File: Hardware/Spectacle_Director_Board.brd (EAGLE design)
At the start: 25.4 x 55.9 mm, 57 parts, among them J1 AUDIO-JACK3, J2 CORTEX_DEBUGPTH, Q1 2N7002PW, Q2 2N7002PW, U3 AP2112K-3.3V, U4 ATSAMD21G-A, U5 W25Q32FVSS

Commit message: Cleaning up schematic
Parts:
- TP1: value TEST-POINT3X5 -> TP-SWDIO
- TP2: value TEST-POINT3X5 -> TP-SWCLK
- TP3: value TEST-POINT3X5 -> TP-!RESET!
- TP4: value TEST-POINT3X5 -> TP-3.3V
- TP5: value TEST-POINT3X5 -> TP-GND
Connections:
- removed net A0: U4.3
- removed net A1: U4.7
- removed net A2: U4.8
- removed net A3: U4.9
- removed net A5: U4.47
- removed net AREF: U4.4
- removed net D11: U4.25
- removed net D2: U4.23
- removed net D5: U4.24
- removed net PB22: U4.37
- removed net PB23: U4.38
- removed net USB_HOST_EN: U4.41
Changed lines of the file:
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@@
 <layer number="47" name="Measures" color="7" fill="1" visible="no" active="yes"/>
 <layer number="48" name="Document" color="7" fill="1" visible="no" active="yes"/>
-<layer number="49" name="Reference" color="7" fill="1" visible="yes" active="yes"/>
+<layer number="49" name="Reference" color="7" fill="1" visible="no" active="yes"/>
 <layer number="51" name="tDocu" color="6" fill="1" visible="yes" active="yes"/>
 <layer number="52" name="bDocu" color="7" fill="1" visible="no" active="yes"/>
@@
 <attribute name="PROD_ID" value="RES-07828" x="-8.255" y="41.91" size="1.778" layer="27" font="vector" ratio="15" display="off"/>
 </element>
-<element name="TP1" library="SparkFun-Connectors" package="PAD.03X.05" value="TEST-POINT3X5" x="3.683" y="28.575" rot="MR0"/>
-<element name="TP2" library="SparkFun-Connectors" package="PAD.03X.05" value="TEST-POINT3X5" x="5.588" y="28.575" rot="MR0"/>
-<element name="TP3" library="SparkFun-Connectors" package="PAD.03X.05" value="TEST-POINT3X5" x="7.493" y="28.575" rot="MR0"/>
+<element name="TP1" library="SparkFun-Connectors" package="PAD.03X.05" value="TP-SWDIO" x="3.683" y="28.575" rot="MR0"/>
+<element name="TP2" library="SparkFun-Connectors" package="PAD.03X.05" value="TP-SWCLK" x="5.588" y="28.575" rot="MR0"/>
+<element name="TP3" library="SparkFun-Connectors" package="PAD.03X.05" value="TP-!RESET!" x="7.493" y="28.575" rot="MR0"/>
 <element name="LOGO3" library="SparkFun-Aesthetics" package="SFE_LOGO_FLAME_COPPER_EXPOSED_.2" value="SFE_LOGO_FLAME.2EXP" x="11.43" y="1.27" rot="R90"/>
 <element name="U$1" library="SparkFun-Aesthetics" package="ORDERING_INSTRUCTIONS" value="" x="-16.51" y="-24.13"/>
-<element name="TP4" library="SparkFun-Connectors" package="PAD.03X.05" value="TEST-POINT3X5" x="1.778" y="28.575" rot="MR0"/>
-<element name="TP5" library="SparkFun-Connectors" package="PAD.03X.05" value="TEST-POINT3X5" x="9.398" y="28.575" rot="MR0"/>
+<element name="TP4" library="SparkFun-Connectors" package="PAD.03X.05" value="TP-3.3V" x="1.778" y="28.575" rot="MR0"/>
+<element name="TP5" library="SparkFun-Connectors" package="PAD.03X.05" value="TP-GND" x="9.398" y="28.575" rot="MR0"/>
 <element name="J2" library="SparkFun-Connectors" package="2X5-PTH-1.27MM" value="CORTEX_DEBUGPTH" x="5.588" y="25.908"/>
 </elements>
@@
 <wire x1="13.5024" y1="41.4678" x2="13.2334" y2="41.1988" width="0.2032" layer="16"/>
 </signal>
-<signal name="D2">
-<contactref element="U4" pad="23"/>
-</signal>
-<signal name="D5">
-<contactref element="U4" pad="24"/>
-</signal>
 <signal name="D6_BTN2">
 <contactref element="U4" pad="29"/>
@@
 <wire x1="16.72" y1="29.2794" x2="16.72" y2="31.31" width="0.2032" layer="1"/>
 </signal>
-<signal name="A3">
-<contactref element="U4" pad="9"/>
-</signal>
-<signal name="A2">
-<contactref element="U4" pad="8"/>
-</signal>
-<signal name="A1">
-<contactref element="U4" pad="7"/>
-</signal>
-<signal name="A0">
-<contactref element="U4" pad="3"/>
-</signal>
 <signal name="D12_BTN1">
 <contactref element="U4" pad="28"/>
@@
 <wire x1="5.987" y1="19.52" x2="5.9996" y2="19.5326" width="0.2032" layer="1"/>
 <wire x1="5.9996" y1="19.5326" x2="9.652" y2="19.5326" width="0.2032" layer="1"/>
-</signal>
-<signal name="D11">
-<contactref element="U4" pad="25"/>
 </signal>
 <signal name="SWCLK">
@@
 <via x="6.9596" y="18.6944" extent="1-16" drill="0.381"/>
 </signal>
-<signal name="USB_HOST_EN">
-<contactref element="U4" pad="41"/>
-</signal>
 <signal name="RX_LED">
 <contactref element="U4" pad="48"/>
@@
 <wire x1="22.86" y1="47.383" x2="22.86" y2="46.3169" width="0.2032" layer="1"/>
 </signal>
-<signal name="AREF">
-<contactref element="U4" pad="4"/>
-</signal>
 <signal name="A4_FLASH!WP!">
 <contactref element="U4" pad="10"/>
@@
 <wire x1="15.4686" y1="25.3238" x2="16.0274" y2="24.765" width="0.2032" layer="1"/>
 <wire x1="17.0688" y1="24.765" x2="16.0274" y2="24.765" width="0.2032" layer="1"/>
-</signal>
-<signal name="A5">
-<contactref element="U4" pad="47"/>
 </signal>
 <signal name="SPI_MISO">
@@
 <wire x1="20.5232" y1="39.624" x2="20.5232" y2="40.64" width="0.2032" layer="1"/>
 </signal>
-<signal name="PB22">
-<contactref element="U4" pad="37"/>
-</signal>
-<signal name="PB23">
-<contactref element="U4" pad="38"/>
-</signal>
 <signal name="N$9">

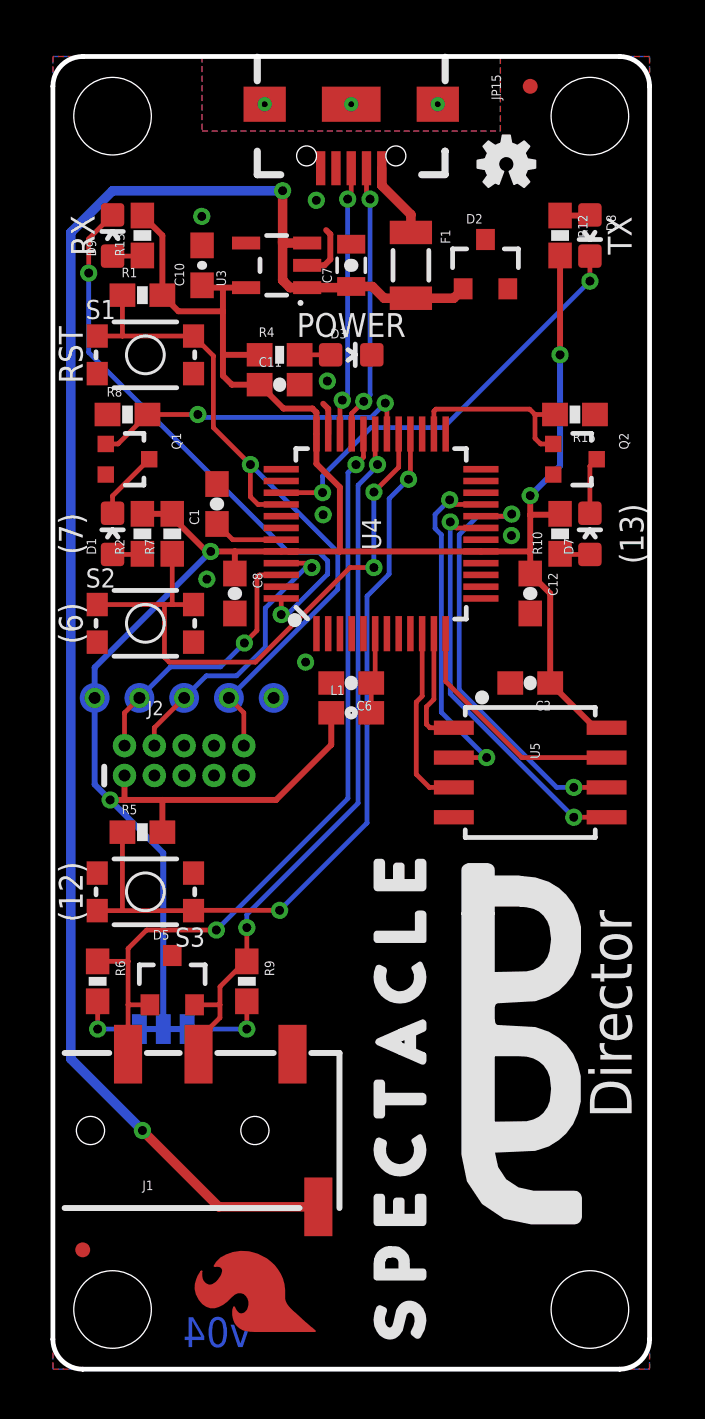
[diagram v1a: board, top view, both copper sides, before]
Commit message: Optimizing routing
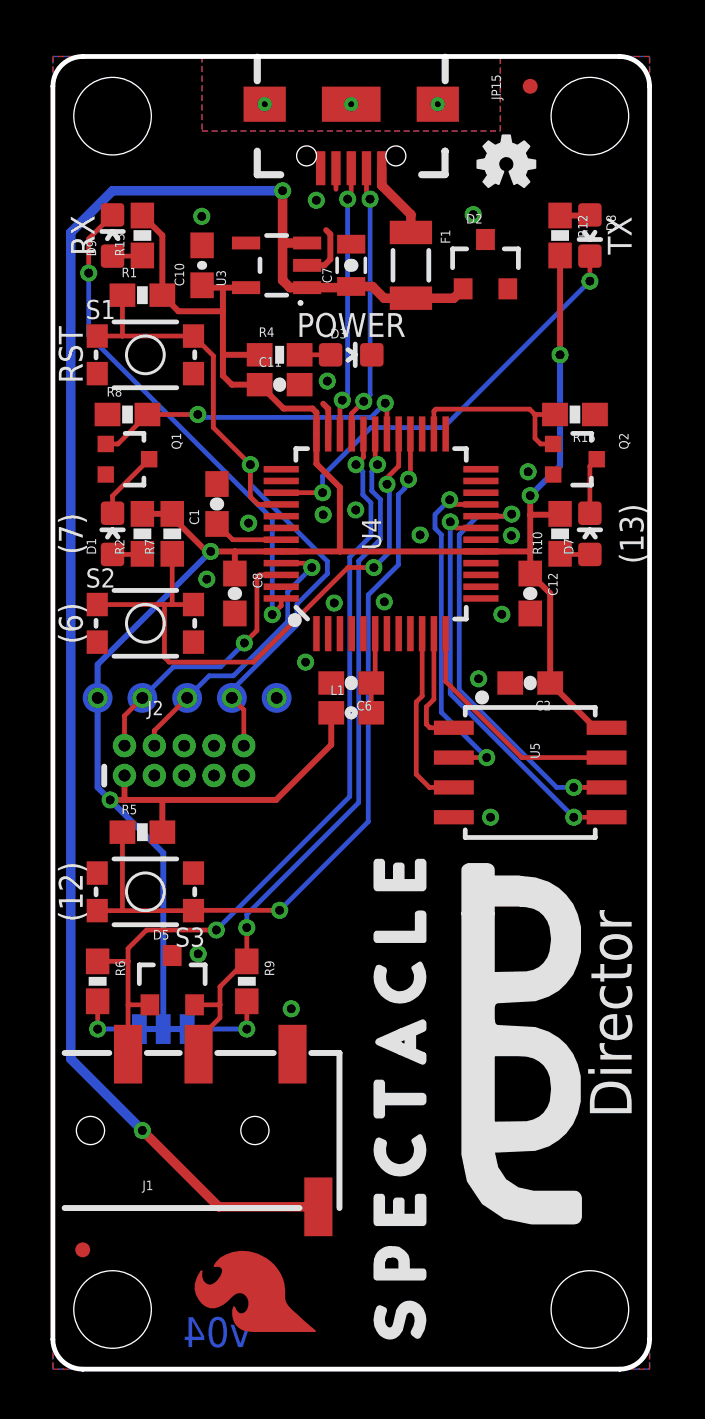
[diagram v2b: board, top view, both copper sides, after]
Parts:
- moved TP5 0.13 mm to (9.53, 28.6)
- moved TP1 0.13 mm to (3.81, 28.6)
- moved TP4 0.13 mm to (1.91, 28.6)
- moved TP2 0.13 mm to (5.71, 28.6)
- moved TP3 0.13 mm to (7.62, 28.6)
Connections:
- new net USB_ID: JP15.ID
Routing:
- net RX_LED: track 24.1 -> 21.5 mm
- net USB_ID: track 0.00 -> 0.90 mm
- net SCL: track 34.5 -> 35.0 mm
- net GND: vias 8 -> 20
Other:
- board text added: "!R!"
- board text added: "C"
- board text added: "D"
- board text added: "G"
- board text added: "V"

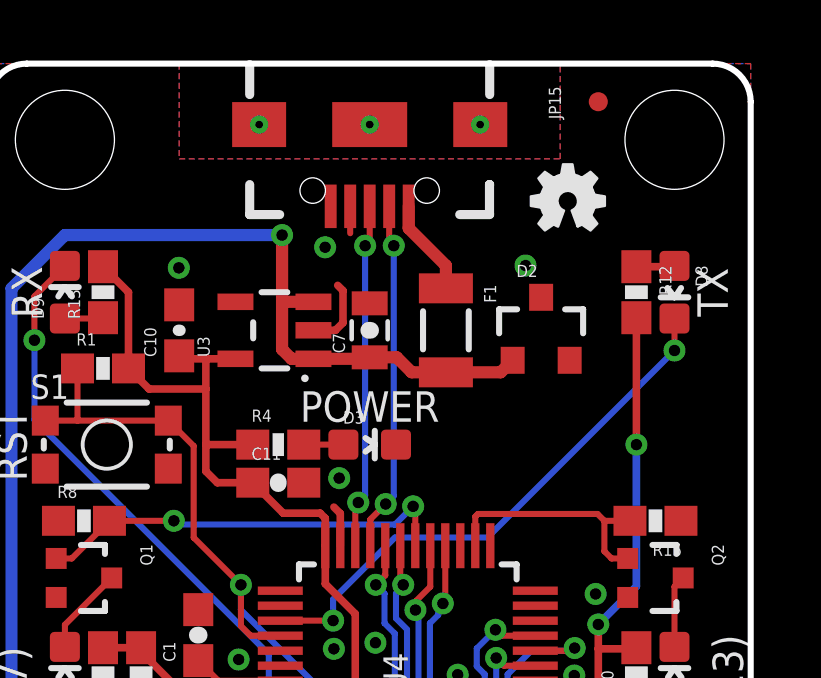
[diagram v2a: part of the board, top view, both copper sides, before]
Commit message: Adjusting some silkscreen.
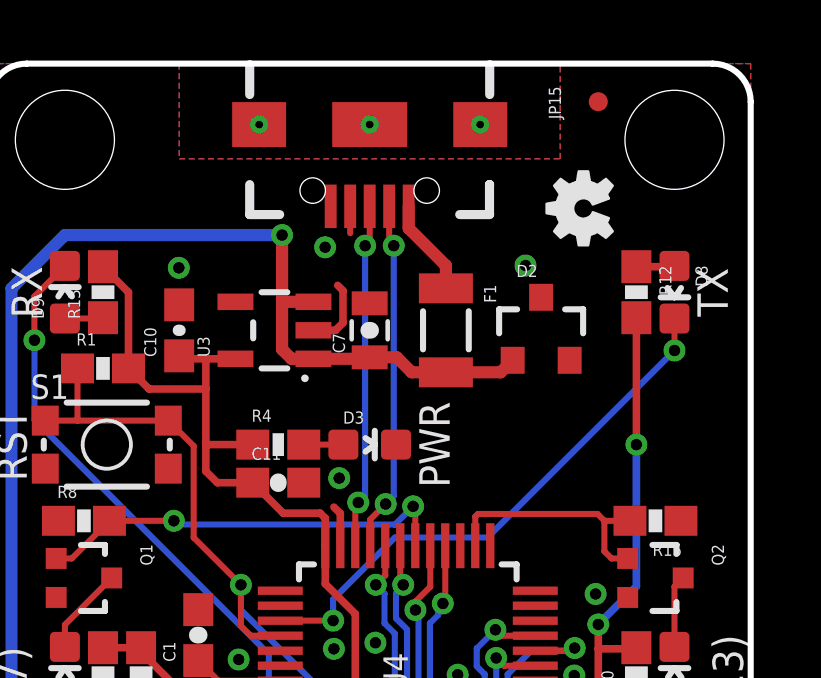
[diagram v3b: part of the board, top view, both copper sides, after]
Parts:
- moved LOGO2 0.57 mm to (19.8, 51.1), turned to 90 degrees
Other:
- board text added: "PWR"
- board text removed: "POWER"
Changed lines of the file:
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@@
 <text x="1.778" y="48.26" size="1.016" layer="21" font="vector" ratio="15" rot="R90" align="bottom-center">RX</text>
 <text x="23.622" y="48.26" size="1.016" layer="21" font="vector" ratio="15" rot="R270" align="bottom-center">TX</text>
-<text x="12.7" y="43.942" size="1.016" layer="21" font="vector" ratio="15" align="bottom-center">POWER</text>
+<text x="14.351" y="43.18" size="1.016" layer="21" font="vector" ratio="15" rot="R270" align="bottom-center">PWR</text>
 <text x="1.905" y="29.337" size="0.889" layer="22" font="vector" ratio="15" rot="MR90" align="center-left">V</text>
 <text x="3.81" y="29.337" size="0.889" layer="22" font="vector" ratio="15" rot="MR90" align="center-left">D</text>
@@
 </element>
 <element name="LOGO1" library="SparkFun-Aesthetics" package="SFE_LOGO_NAME_.2" value="SFE_LOGO_NAME.2_INCH" x="23.622" y="44.577" rot="MR0"/>
-<element name="LOGO2" library="SparkFun-Aesthetics" package="OSHW-LOGO-MINI" value="OSHW-LOGOMINI" x="19.304" y="51.308"/>
+<element name="LOGO2" library="SparkFun-Aesthetics" package="OSHW-LOGO-MINI" value="OSHW-LOGOMINI" x="19.812" y="51.054" rot="R90"/>
 <element name="D2" library="SparkFun-DiscreteSemi" package="SOT23-3" value="PESD1CAN" x="18.415" y="46.99">
 <attribute name="PROD_ID" value="DIO-12501" x="18.415" y="46.99" size="1.778" layer="27" font="vector" ratio="15" display="off"/>
